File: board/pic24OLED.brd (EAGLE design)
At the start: 100 x 80 mm, 10 parts, among them U1 PIC24FJ64GA002T-I/ML

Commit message: Finished up first board draft completely.
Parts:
- removed U$1: THRESISTOR, pic24fj64ga002:THRESISTOR
- added 10KRES: THRESISTOR, pic24fj64ga002:THRESISTOR
- added 10UF, 10UFPWR: THCAP, pic24fj64ga002:THCAP
- added THROBLED: THLED, pic24fj64ga002:THLED
- moved DEBUG 64.4 mm to (79.6, 61.0)
- moved GPIO 31.8 mm to (27.7, 61.0)
- moved OSCILLATOR 10.2 mm to (75.6, 27.2), turned to 180 degrees
- moved LCD 2.96 mm to (53.8, 73.7)
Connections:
- new net N$22: 10UF.P$1, U1.17
- new net N$23: 10UF.P$2, U1.16
- net GND: now also 10UFPWR.P$2
- net N$13: now also 10KRES.P$2; no longer U$1.P$2
- net N$14: now also THROBLED.GND
- net VDD: now also 10KRES.P$1, 10UFPWR.P$1, THROBLED.PWR, U1.5; no longer U$1.P$1
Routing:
- net N$14: track 0.00 -> 64.0 mm, vias 0 -> 2
- net N$20: track 0.00 -> 62.0 mm, vias 0 -> 2
- net N$16: track 0.00 -> 61.6 mm, vias 0 -> 1
- net N$17: track 0.00 -> 54.6 mm
- net N$19: track 0.00 -> 52.5 mm, vias 0 -> 1
- net N$21: track 0.00 -> 50.9 mm, vias 0 -> 2
- net N$22: track 0.00 -> 50.6 mm, vias 0 -> 1
- net VDD: track 113.9 -> 159.1 mm, vias 1 -> 3
- net N$15: track 0.00 -> 43.9 mm, vias 0 -> 2
- net N$18: track 0.00 -> 41.1 mm, vias 0 -> 2
- net N$13: track 43.2 -> 78.6 mm, vias 1 -> 2
- net N$7: track 50.4 -> 20.6 mm
- net GND: track 135.1 -> 163.0 mm
- net N$2: track 26.4 -> 49.9 mm, vias 0 -> 2
- net N$6: track 27.4 -> 49.3 mm, vias 0 -> 2
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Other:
- board size 100 x 80 mm -> 64 x 64 mm
- board text added: "GND"
- board text added: "Loubear - June 2019 louisbarrett98@gmail.com"
- board text added: "RA0"
- board text added: "RA1"
- board text added: "RA2"
- board text added: "RA3"
- board text added: "RB10"
- board text added: "RB11"
- board text added: "RB2"
- board text added: "RB3"
- board text added: "VDD"

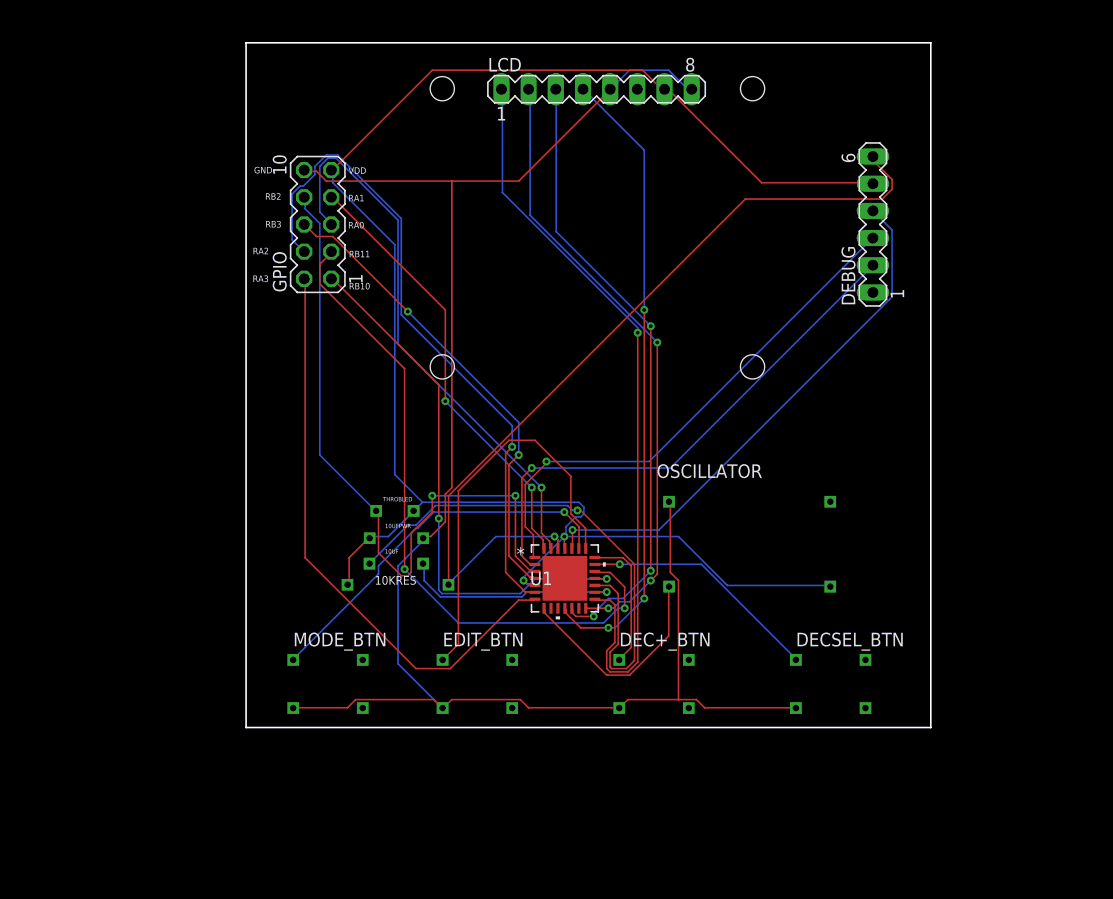
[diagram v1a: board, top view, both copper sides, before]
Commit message: Board design v1.1
Used PIC layout I can actually solder. Moved some things around for easier access and made holes bigger.
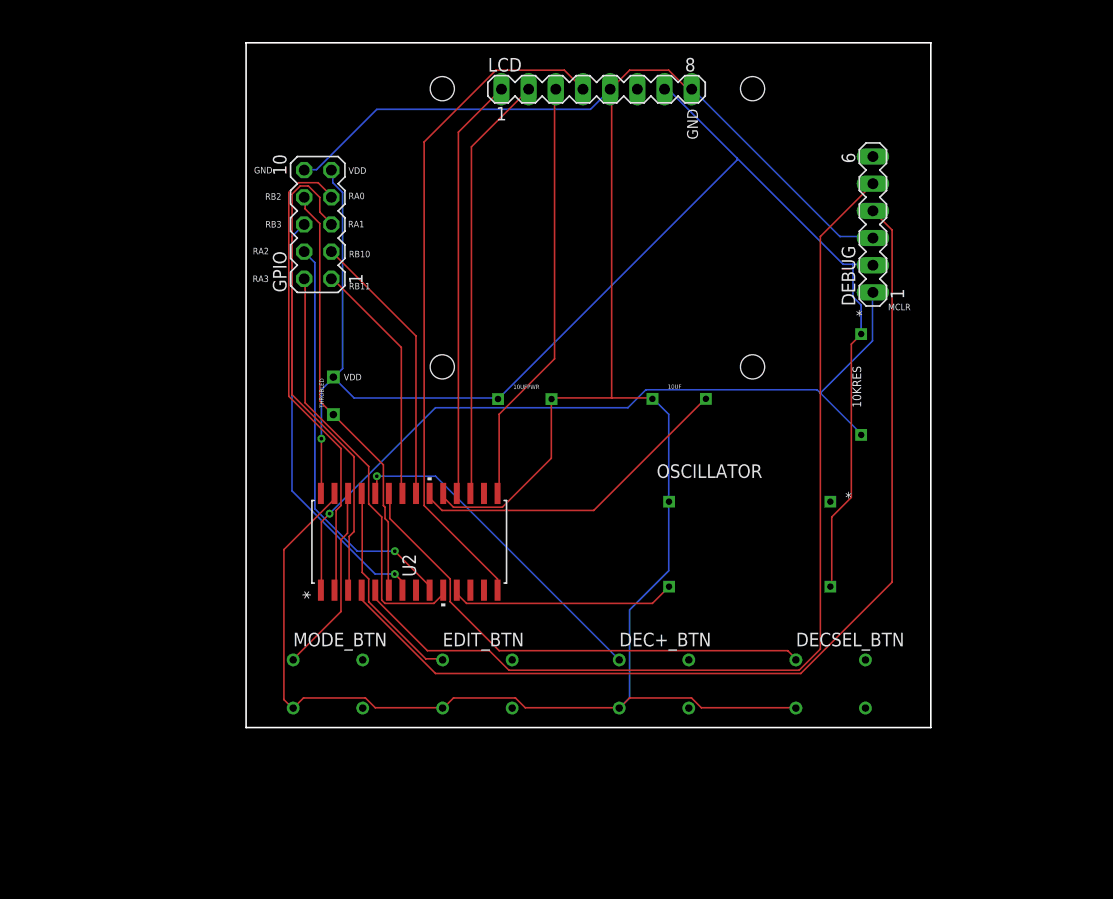
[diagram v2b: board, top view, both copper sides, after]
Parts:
- removed U1: PIC24FJ64GA002T-I/ML, pic24fj64ga002:QFN28_6X6MC
- added U2: PIC24FJ64GA002-I/SO, pic24fj64ga002:SOIC28-W_MC
- moved 10KRES 50.0 mm to (78.5, 41.4), turned to 90 degrees
- moved 10UF 30.6 mm to (59.0, 44.7)
- moved 10UFPWR 17.7 mm to (44.5, 44.7)
- moved THROBLED 9.85 mm to (29.2, 43.2), turned to 90 degrees
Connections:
- removed net N$22: 10UF.P$1, U1.17
- removed net N$23: 10UF.P$2, U1.16
- net GND: now also 10UF.P$1, DEBUG.3, U2.19, U2.27
- net N$1: now also 10KRES.P$1, DEBUG.1, U2.1; no longer MODE_BTN.1, U1.23
- net N$10: now also LCD.1, U2.18; no longer LCD.2, U1.14
- net N$11: now also 10UF.P$2, U2.20; no longer LCD.3, U1.12
- net N$12: now also GPIO.6, U2.7; no longer LCD.4, U1.11
- net N$13: now also OSCILLATOR.SIG, U2.11; no longer 10KRES.P$2, DEBUG.6, U1.26
- net N$14: now also U2.6; no longer U1.3
- net N$15: now also DEBUG.4, U2.4; no longer GPIO.6, U1.4
- net N$16: now also DEBUG.5, U2.5; no longer GPIO.4, U1.6
- net N$17: now also U2.10; no longer U1.7
- net N$18: now also U2.2; no longer U1.28
- net N$19: now also U2.3; no longer U1.27
- net N$2: now also GPIO.4, U2.9; no longer DEBUG.2, U1.2
- net N$20: now also U2.21; no longer U1.19
- net N$21: now also U2.22; no longer U1.18
- net N$3: now also MODE_BTN.1, U2.26; no longer EDIT_BTN.1, U1.22
- net N$4: now also EDIT_BTN.1, U2.25; no longer DEC+_BTN.1, U1.21
- net N$5: now also DEC+_BTN.1, U2.24; no longer DECSEL_BTN.1, U1.20
- net N$6: now also DECSEL_BTN.1, U2.23; no longer DEBUG.3, U1.1
- net N$7: now also LCD.4, U2.14; no longer OSCILLATOR.SIG, U1.8
- net N$8: now also LCD.3, U2.15; no longer DEBUG.4, U1.24
- net N$9: now also LCD.2, U2.17; no longer LCD.1, U1.15
- net VDD: now also 10KRES.P$2, DEBUG.2, U2.28; no longer 10KRES.P$1, DEBUG.5, U1.25, U1.5
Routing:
- net GND: track 163.0 -> 223.6 mm
- net N$13: track 78.6 -> 21.3 mm, vias 2 -> 0
- net N$22: track 50.6 -> 0.00 mm, vias 1 -> 0
- net N$15: track 43.9 -> 92.3 mm, vias 2 -> 0
- net N$7: track 20.6 -> 63.1 mm
- net N$1: track 35.5 -> 75.2 mm
- net N$20: track 62.0 -> 25.9 mm, vias 2 -> 0
- net N$9: track 70.6 -> 40.0 mm, vias 1 -> 0
- net N$16: track 61.6 -> 91.6 mm, vias 1 -> 0
- net N$21: track 50.9 -> 22.9 mm, vias 2 -> 0
- net N$11: track 58.5 -> 31.1 mm, vias 3 -> 0
- net N$14: track 64.0 -> 40.0 mm, vias 2 -> 0
- net VDD: track 159.1 -> 137.5 mm, vias 3 -> 1
- net N$23: track 20.7 -> 0.00 mm, vias 1 -> 0
- net N$3: track 37.6 -> 17.7 mm
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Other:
- board text added: "*"
- board text added: "Loubear - July 2019 v1.1 louisbarrett98@gmail.com"
- board text added: "MCLR"
- board text removed: "Loubear - June 2019 louisbarrett98@gmail.com"
